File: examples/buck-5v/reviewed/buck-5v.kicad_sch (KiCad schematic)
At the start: 11 parts, among them J1 12V IN, J2 5V OUT, U1 LM2596S-5

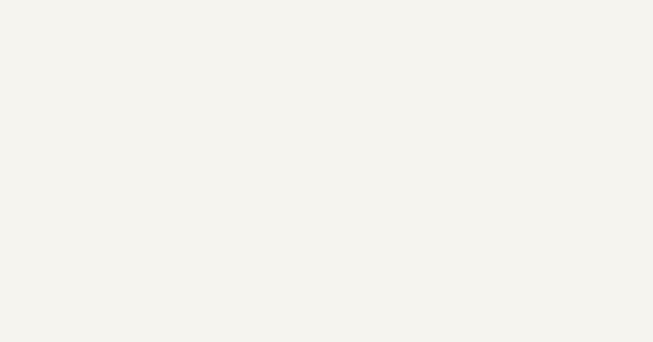
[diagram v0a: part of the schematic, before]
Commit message: Relieve the pads, fillet the joints, and give the board its screw holes
Three of the reviewer's manufacturing points, and they largely fall out
of the one before it - once KiCad fills the plane, the thermal relief it
was already asked for in the file actually appears.

**Thermal relief.** The zones said thermal all along; our own filler
ignored it and flooded every land solid. KiCad's does not, so every
through-hole ground pad now sits in a gap bridged by four spokes and an
iron can bring the joint up without heating a hundred square millimetres
of copper. `layout.solid_pad_connection` reports the setting when a
board turns it off: drilled pads only, because a surface pad reflows in
an oven that is heating the plane anyway and flooding it is often the
better thermal answer.

**Teardrops.** A track entering a land is a step change in width, and a
step change is where copper tears - the connector gets levered on and
off, the drill wanders, and the crack starts at the corner. `_teardrops`
replaces the first stretch of each run with a three-step taper into the
land, checked against its neighbours before it is kept, so a fillet
never eats the clearance a fine-pitch escape needs. It *replaces* rather
than overlays: laying the taper on top of the run drew the same copper
twice, and `route.acute_angle` reported all thirty of them, correctly.
`route.mixed_track_widths` learns what a fillet looks like so a properly
filleted board does not read as one nobody decided the width of.

**Mounting holes.** Four M3 holes near the corners, placed before the
router runs because they are obstacles, and slid along the edges or a
little inboard where a connector body has the corner - the motor board
and the op-amp take three, which is what those floorplans have room for.
Grounded on the motor driver, whose chassis is metal and part of the
shield, plain on the rest: bonding the enclosure to the reference is the
enclosure's decision, not the board's.

Two things that fell out of placing par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
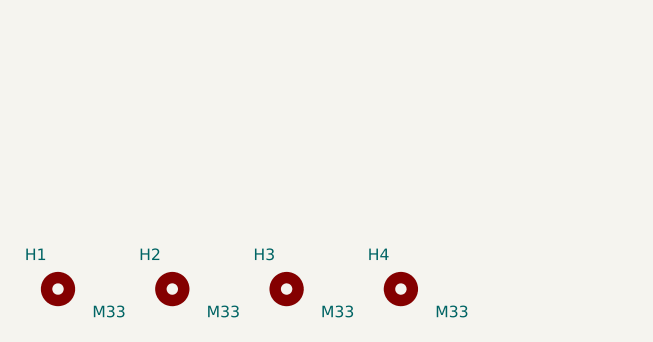
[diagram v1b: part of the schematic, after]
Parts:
- added H1, H2, H3, H4: M33, MountingHole:MountingHole_3.2mm_M3, symbol Mechanical:MountingHole
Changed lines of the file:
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@@
     (instances (project "buck-5v" (path "/ec98644d-848c-5056-a4cb-c829189be5c3" (reference "J2") (unit 1))))
+  )
+  (symbol (lib_id "Mechanical:MountingHole") (at 25.4 170.18 0.0) (unit 1)
+    (exclude_from_sim no) (in_bom yes) (on_board yes) (dnp no)
+    (property "Reference" "H1" (at 24.13 166.37 0) (effects (font (size 1.27 1.27)) (justify right)))
+    (property "Value" "M33" (at 29.21 172.72 0) (effects (font (size 1.27 1.27)) (justify left)))
+    (property "Footprint" "MountingHole:MountingHole_3.2mm_M3" (at 25.4 170.18 0) (effects (font (size 1.27 1.27)) hide))
+    (property "Datasheet" "~" (at 25.4 170.18 0) (effects (font (size 1.27 1.27)) hide))
+    (property "MPN" "n/a" (at 25.4 170.18 0) (effects (font (size 1.27 1.27)) hide))
+    (property "Manufacturer" "n/a" (at 25.4 170.18 0) (effects (font (size 1.27 1.27)) hide))
+    (instances (project "buck-5v" (path "/ec98644d-848c-5056-a4cb-c829189be5c3" (reference "H1") (unit 1))))
+  )
+  (symbol (lib_id "Mechanical:MountingHole") (at 38.099999999999994 170.18 0.0) (unit 1)
+    (exclude_from_sim no) (in_bom yes) (on_board yes) (dnp no)
+    (property "Reference" "H2" (at 36.83 166.37 0) (effects (font (size 1.27 1.27)) (justify right)))
+    (property "Value" "M33" (at 41.91 172.72 0) (effects (font (size 1.27 1.27)) (justify left)))
+    (property "Footprint" "MountingHole:MountingHole_3.2mm_M3" (at 38.099999999999994 170.18 0) (effects (font (size 1.27 1.27)) hide))
+    (property "Datasheet" "~" (at 38.099999999999994 170.18 0) (effects (font (size 1.27 1.27)) hide))
+    (property "MPN" "n/a" (at 38.099999999999994 170.18 0) (effects (font (size 1.27 1.27)) hide))
+    (property "Manufacturer" "n/a" (at 38.099999999999994 170.18 0) (effects (font (size 1.27 1.27)) hide))
+    (instances (project "buck-5v" (path "/ec98644d-848c-5056-a4cb-c829189be5c3" (reference "H2") (unit 1))))
+  )
+  (symbol (lib_id "Mechanical:MountingHole") (at 50.8 170.18 0.0) (unit 1)
+    (exclude_from_sim no) (in_bom yes) (on_board yes) (dnp no)
+    (property "Reference" "H3" (at 49.53 166.37 0) (effects (font (size 1.27 1.27)) (justify right)))
+    (property "Value" "M33" (at 54.61 172.72 0) (effects (font (size 1.27 1.27)) (justify left)))
+    (property "Footprint" "MountingHole:MountingHole_3.2mm_M3" (at 50.8 170.18 0) (effects (font (size 1.27 1.27)) hide))
+    (property "Datasheet" "~" (at 50.8 170.18 0) (effects (font (size 1.27 1.27)) hide))
+    (property "MPN" "n/a" (at 50.8 170.18 0) (effects (font (size 1.27 1.27)) hide))
+    (property "Manufacturer" "n/a" (at 50.8 170.18 0) (effects (font (size 1.27 1.27)) hide))
+    (instances (project "buck-5v" (path "/ec98644d-848c-5056-a4cb-c829189be5c3" (reference "H3") (unit 1))))
+  )
+  (symbol (lib_id "Mechanical:MountingHole") (at 63.49999999999999 170.18 0.0) (unit 1)
+    (exclude_from_sim no) (in_bom yes) (on_board yes) (dnp no)
+    (property "Reference" "H4" (at 62.23 166.37 0) (effects (font (size 1.27 1.27)) (justify right)))
+    (property "Value" "M33" (at 67.31 172.72 0) (effects (font (size 1.27 1.27)) (justify left)))
+    (property "Footprint" "MountingHole:MountingHole_3.2mm_M3" (at 63.49999999999999 170.18 0) (effects (font (size 1.27 1.27)) hide))
+    (property "Datasheet" "~" (at 63.49999999999999 170.18 0) (effects (font (size 1.27 1.27)) hide))
+    (property "MPN" "n/a" (at 63.49999999999999 170.18 0) (effects (font (size 1.27 1.27)) hide))
+    (property "Manufacturer" "n/a" (at 63.49999999999999 170.18 0) (effects (font (size 1.27 1.27)) hide))
+    (instances (project "buck-5v" (path "/ec98644d-848c-5056-a4cb-c829189be5c3" (reference "H4") (unit 1))))
   )
   (wire (pts (xy 45.72 63.5) (xy 45.72 60.96)) (stroke (width 0) (type default)))

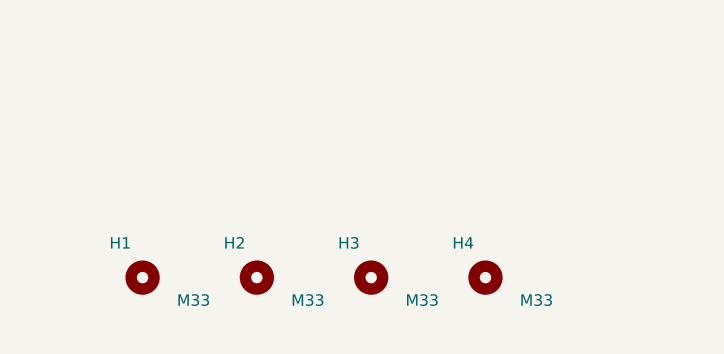
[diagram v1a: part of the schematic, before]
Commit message: Give the assembly machine something to aim at
Fiducials: three copper dots in bare mask windows, near three different
corners so a pick-and-place gets rotation as well as offset. It aligns
to the board, not to the drawing - without them it has only the routed
outline, cut to a tolerance ten times looser than the placement a 0.5 mm
pitch part is asking for. `fab.no_fiducials` reports a fine-pitch board
that has none, as context rather than as a fault: plenty of boards are
built one at a time with tweezers.

They share the corner search with the mounting holes, which is where
this found a real bug: `_courtyard_box` read lines and rectangles only,
and a mounting hole draws its courtyard as one circle - so every hole
measured as taking up no room at all, and the first three fiducials
landed on top of three screw holes. Circles and arcs count now.

Co-Authored-By: Claude Fable 5 <noreply@anthropic.com>
Claude-Session: https://claude.ai/code/session_01DUj7Ltu92tWg159mCSacwY
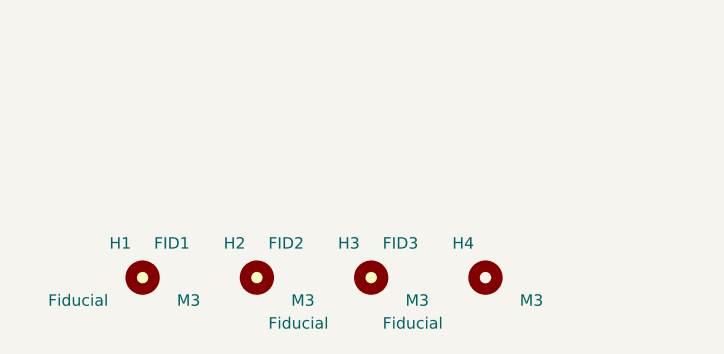
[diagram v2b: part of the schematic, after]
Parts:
- added FID1, FID2, FID3: Fiducial, Fiducial:Fiducial_1mm_Mask2mm, symbol Mechanical:Fiducial
- H1, H2, H3, H4: value M33 -> M3
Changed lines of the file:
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@@
     (exclude_from_sim no) (in_bom yes) (on_board yes) (dnp no)
     (property "Reference" "H1" (at 24.13 166.37 0) (effects (font (size 1.27 1.27)) (justify right)))
-    (property "Value" "M33" (at 29.21 172.72 0) (effects (font (size 1.27 1.27)) (justify left)))
+    (property "Value" "M3" (at 29.21 172.72 0) (effects (font (size 1.27 1.27)) (justify left)))
     (property "Footprint" "MountingHole:MountingHole_3.2mm_M3" (at 25.4 170.18 0) (effects (font (size 1.27 1.27)) hide))
     (property "Datasheet" "~" (at 25.4 170.18 0) (effects (font (size 1.27 1.27)) hide))
@@
     (exclude_from_sim no) (in_bom yes) (on_board yes) (dnp no)
     (property "Reference" "H2" (at 36.83 166.37 0) (effects (font (size 1.27 1.27)) (justify right)))
-    (property "Value" "M33" (at 41.91 172.72 0) (effects (font (size 1.27 1.27)) (justify left)))
+    (property "Value" "M3" (at 41.91 172.72 0) (effects (font (size 1.27 1.27)) (justify left)))
     (property "Footprint" "MountingHole:MountingHole_3.2mm_M3" (at 38.099999999999994 170.18 0) (effects (font (size 1.27 1.27)) hide))
     (property "Datasheet" "~" (at 38.099999999999994 170.18 0) (effects (font (size 1.27 1.27)) hide))
@@
     (exclude_from_sim no) (in_bom yes) (on_board yes) (dnp no)
     (property "Reference" "H3" (at 49.53 166.37 0) (effects (font (size 1.27 1.27)) (justify right)))
-    (property "Value" "M33" (at 54.61 172.72 0) (effects (font (size 1.27 1.27)) (justify left)))
+    (property "Value" "M3" (at 54.61 172.72 0) (effects (font (size 1.27 1.27)) (justify left)))
     (property "Footprint" "MountingHole:MountingHole_3.2mm_M3" (at 50.8 170.18 0) (effects (font (size 1.27 1.27)) hide))
     (property "Datasheet" "~" (at 50.8 170.18 0) (effects (font (size 1.27 1.27)) hide))
@@
     (exclude_from_sim no) (in_bom yes) (on_board yes) (dnp no)
     (property "Reference" "H4" (at 62.23 166.37 0) (effects (font (size 1.27 1.27)) (justify right)))
-    (property "Value" "M33" (at 67.31 172.72 0) (effects (font (size 1.27 1.27)) (justify left)))
+    (property "Value" "M3" (at 67.31 172.72 0) (effects (font (size 1.27 1.27)) (justify left)))
     (property "Footprint" "MountingHole:MountingHole_3.2mm_M3" (at 63.49999999999999 170.18 0) (effects (font (size 1.27 1.27)) hide))
     (property "Datasheet" "~" (at 63.49999999999999 170.18 0) (effects (font (size 1.27 1.27)) hide))
@@
     (instances (project "buck-5v" (path "/ec98644d-848c-5056-a4cb-c829189be5c3" (reference "H4") (unit 1))))
   )
+  (symbol (lib_id "Mechanical:Fiducial") (at 25.4 170.18 0.0) (unit 1)
+    (exclude_from_sim no) (in_bom yes) (on_board yes) (dnp no)
+    (property "Reference" "FID1" (at 26.67 166.37 0) (effects (font (size 1.27 1.27)) (justify left)))
+    (property "Value" "Fiducial" (at 21.59 172.72 0) (effects (font (size 1.27 1.27)) (justify right)))
+    (property "Footprint" "Fiducial:Fiducial_1mm_Mask2mm" (at 25.4 170.18 0) (effects (font (size 1.27 1.27)) hide))
+    (property "Datasheet" "~" (at 25.4 170.18 0) (effects (font (size 1.27 1.27)) hide))
+    (property "MPN" "n/a" (at 25.4 170.18 0) (effects (font (size 1.27 1.27)) hide))
+    (property "Manufacturer" "n/a" (at 25.4 170.18 0) (effects (font (size 1.27 1.27)) hide))
+    (instances (project "buck-5v" (path "/ec98644d-848c-5056-a4cb-c829189be5c3" (reference "FID1") (unit 1))))
+  )
+  (symbol (lib_id "Mechanical:Fiducial") (at 38.099999999999994 170.18 0.0) (unit 1)
+    (exclude_from_sim no) (in_bom yes) (on_board yes) (dnp no)
+    (property "Reference" "FID2" (at 39.37 166.37 0) (effects (font (size 1.27 1.27)) (justify left)))
+    (property "Value" "Fiducial" (at 39.37 175.26 0) (effects (font (size 1.27 1.27)) (justify left)))
+    (property "Footprint" "Fiducial:Fiducial_1mm_Mask2mm" (at 38.099999999999994 170.18 0) (effects (font (size 1.27 1.27)) hide))
+    (property "Datasheet" "~" (at 38.099999999999994 170.18 0) (effects (font (size 1.27 1.27)) hide))
+    (property "MPN" "n/a" (at 38.099999999999994 170.18 0) (effects (font (size 1.27 1.27)) hide))
+    (property "Manufacturer" "n/a" (at 38.099999999999994 170.18 0) (effects (font (size 1.27 1.27)) hide))
+    (instances (project "buck-5v" (path "/ec98644d-848c-5056-a4cb-c829189be5c3" (reference "FID2") (unit 1))))
+  )
+  (symbol (lib_id "Mechanical:Fiducial") (at 50.8 170.18 0.0) (unit 1)
+    (exclude_from_sim no) (in_bom yes) (on_board yes) (dnp no)
+    (property "Reference" "FID3" (at 52.07 166.37 0) (effects (font (size 1.27 1.27)) (justify left)))
+    (property "Value" "Fiducial" (at 52.07 175.26 0) (effects (font (size 1.27 1.27)) (justify left)))
+    (property "Footprint" "Fiducial:Fiducial_1mm_Mask2mm" (at 50.8 170.18 0) (effects (font (size 1.27 1.27)) hide))
+    (property "Datasheet" "~" (at 50.8 170.18 0) (effects (font (size 1.27 1.27)) hide))
+    (property "MPN" "n/a" (at 50.8 170.18 0) (effects (font (size 1.27 1.27)) hide))
+    (property "Manufacturer" "n/a" (at 50.8 170.18 0) (effects (font (size 1.27 1.27)) hide))
+    (instances (project "buck-5v" (path "/ec98644d-848c-5056-a4cb-c829189be5c3" (reference "FID3") (unit 1))))
+  )
   (wire (pts (xy 45.72 63.5) (xy 45.72 60.96)) (stroke (width 0) (type default)))

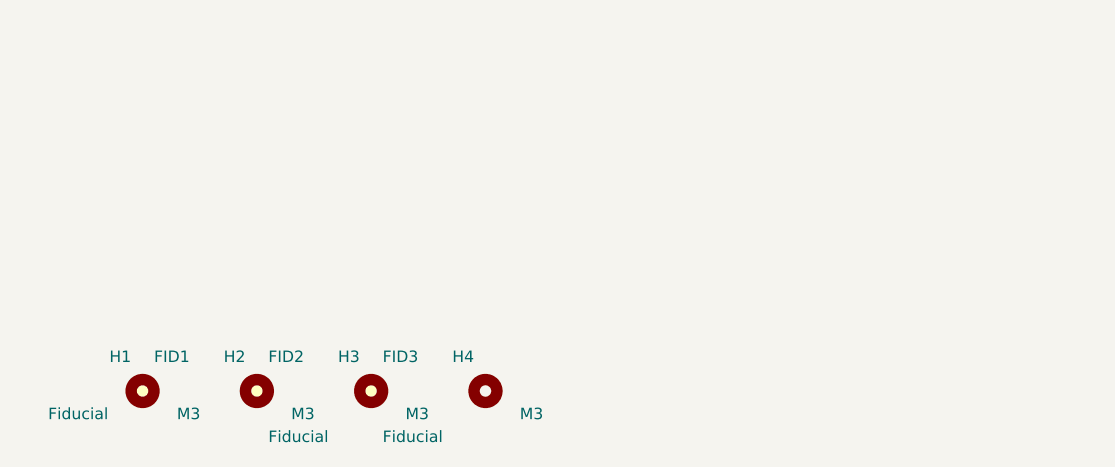
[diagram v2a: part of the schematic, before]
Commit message: Let the new parts sit somewhere sensible, on the board and on the sheet
Placing screw holes and fiducials turned up four things that were wrong
before either existed, all of them about where something is allowed to
go rather than about the parts themselves.

A designator was kept off the pads but not inside the board outline, so
any part at the edge - a connector, and now a hole - had its reference
clipped by the edge. Every board had been carrying one or two of those.

A symbol with no pins leaves no trace in the sheet planner's obstacle
list, because that list is built from pin stubs. The screw holes were
invisible to it and the fiducials landed on top of them. The free-row
search also ran off the right-hand edge of an A4 page and sat over the
title block on the way, which is `readability.outside_page` and
`readability.margin_intrusion` respectively - both real, both now
avoided by bounding the search to the drawing area.

And the bill-of-materials flag is read from the footprint rather than
the symbol library, because the footprint is the side KiCad's parity
check reads and the side the fab agrees with. That retired three
warnings the op-amp board had been carrying since it gained test
points: `Connector:TestPoint` claims to be a BOM line and its own
footprint says otherwise.

All four fast boards pass their gates; the suite is green on 10.0.4.

Co-Authored-By: Claude Fable 5 <noreply@anthropic.com>
Claude-Session: https://claude.ai/code/session_01DUj7Ltu92tWg159mCSacwY
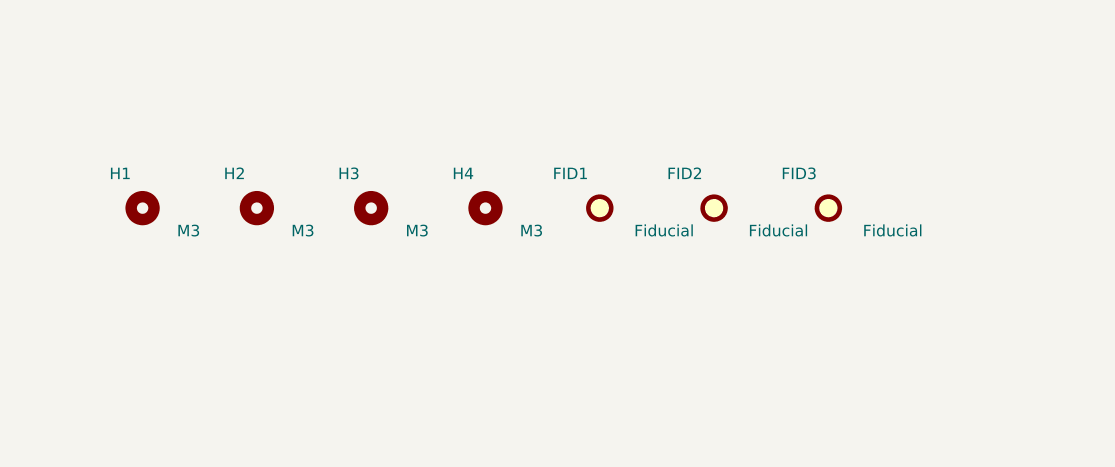
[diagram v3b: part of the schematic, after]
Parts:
- FID1, FID2, FID3, H1, H2, H3, H4: now left out of the parts list
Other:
- moved on the sheet: FID1, FID2, FID3, H1, H2, H3, H4
